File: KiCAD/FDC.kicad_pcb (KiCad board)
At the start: 2 copper layers, 72.6 x 65.5 mm, 24 parts, among them J2 Conn_02x20_Odd_Even, J3 SD_Card, Q1 SSM3K324RLFCT-ND, Q2 SSM3K324RLFCT-ND, U1 SN74LVCC4245ADWR, U2 Pico, U3 SN74LVCC4245ADWR, U4 SN74LVCC4245ADWR, U5 SN74LVCC4245ADWR

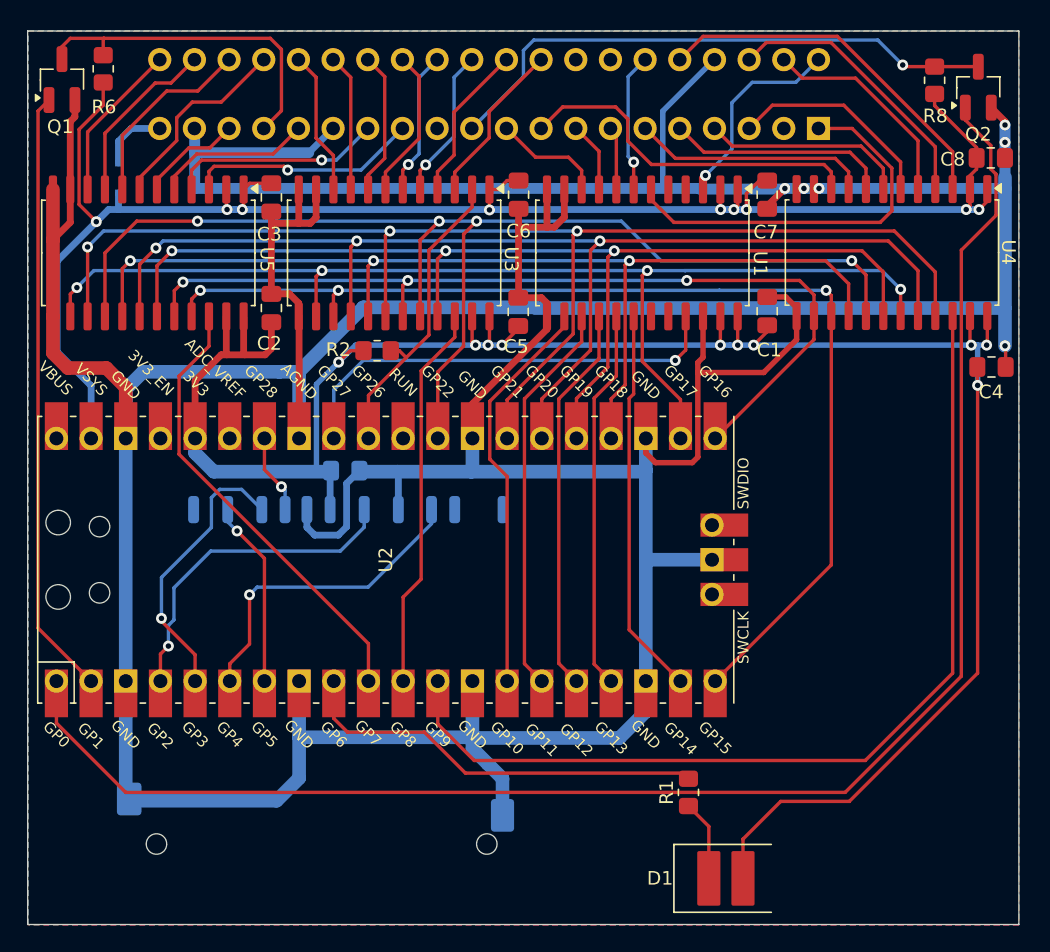
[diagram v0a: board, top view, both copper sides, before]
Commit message: Updates schematic part numbers
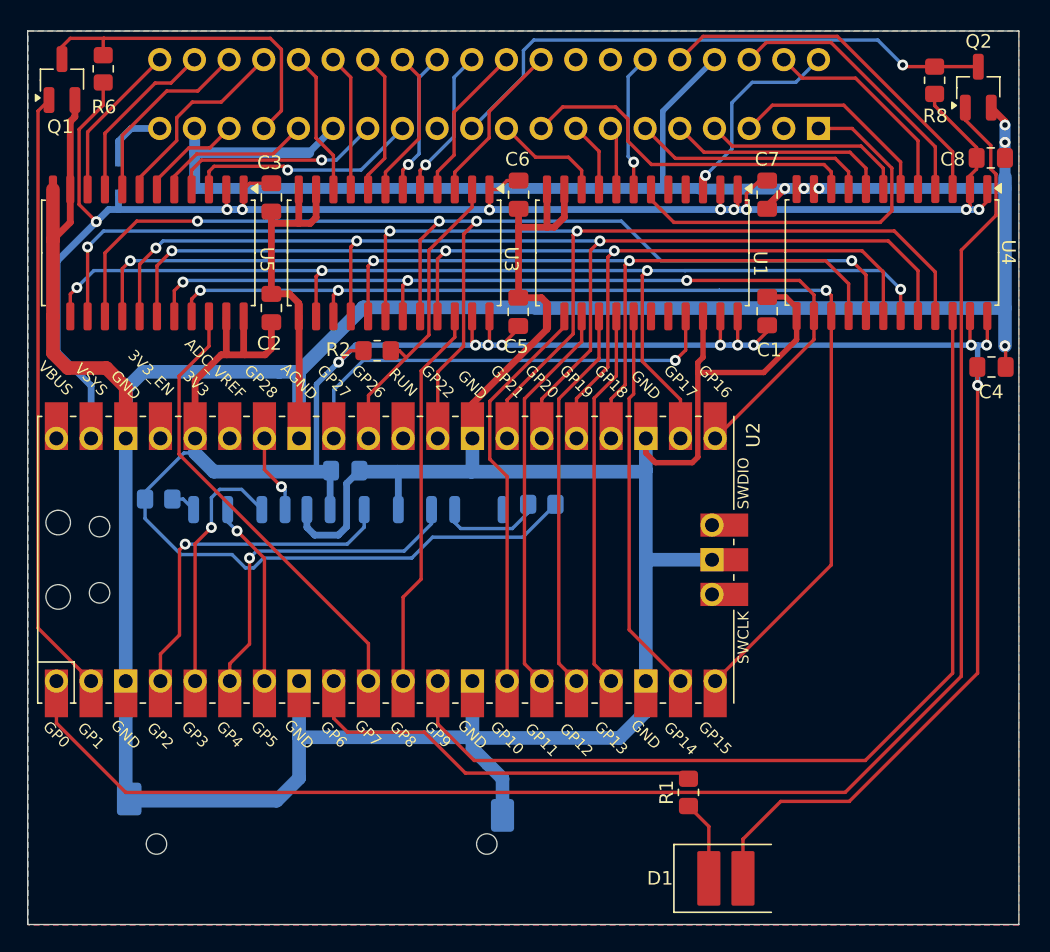
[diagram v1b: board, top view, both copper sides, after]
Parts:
- added R3: 1k, Resistor_SMD:R_0805_2012Metric_Pad1.20x1.40mm_HandSolder, B.Cu at (149.7, 90.8)
- added R4: 1k, Resistor_SMD:R_0805_2012Metric_Pad1.20x1.40mm_HandSolder, B.Cu at (121.7, 90.4)
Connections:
- J3 pad 8: unconnected-(J3-DAT1-Pad8) -> Net-(J3-DAT1)
- J3 pad 9: unconnected-(J3-DAT2-Pad9) -> Net-(J3-DAT2)
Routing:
- net +3V3: track 158.8 -> 199.1 mm
- net Net-(J3-DAT1): track 0.00 -> 7.61 mm
- net /CMD_MOSI: track 20.5 -> 18.5 mm
- net Net-(J3-DAT2): track 0.00 -> 1.88 mm
- net /DAT0_MISO: track 23.4 -> 25.0 mm
- net /CLK_SCLK: track 24.3 -> 25.7 mm
